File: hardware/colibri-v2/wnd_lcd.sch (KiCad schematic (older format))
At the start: 41 parts, among them CN6 Wurth-68715014522-LCD, U12 TSC2046IPWR

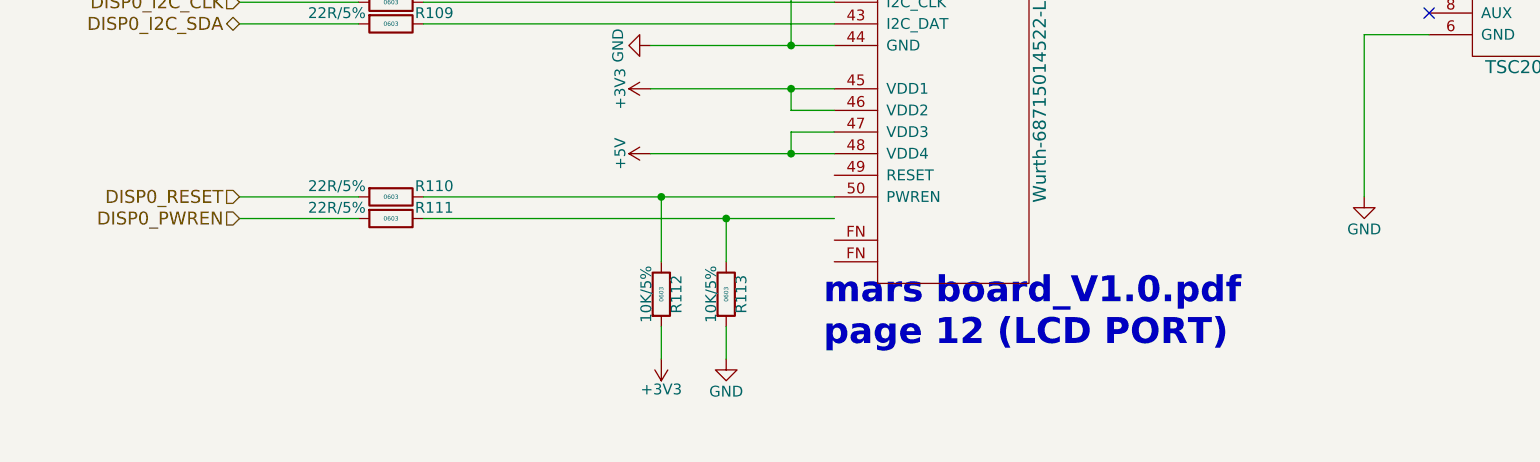
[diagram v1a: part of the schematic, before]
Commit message: Added footprints
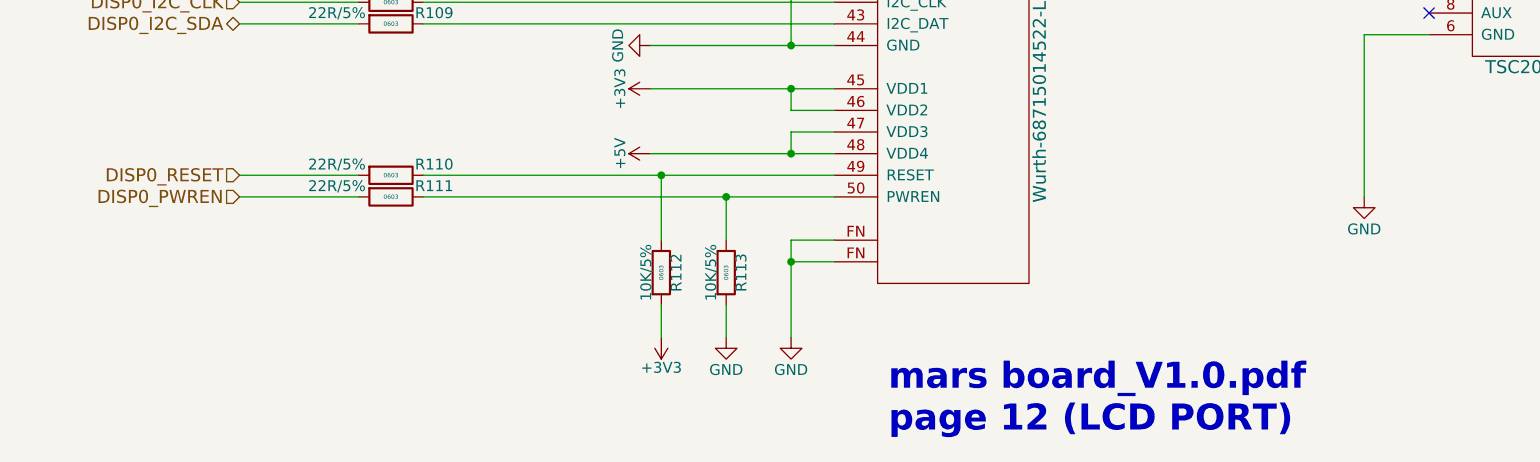
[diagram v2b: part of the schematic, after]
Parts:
- CN6: footprint (none) -> Sigmadrone:68715014522
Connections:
- net GND: now also CN6.FN
- net at CN6.49 (RESET): now also R110.1, R112.1
- net at R111.1, R113.1: now also CN6.50 (PWREN)
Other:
- moved on the sheet: R110, R111, R112, R113
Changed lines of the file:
@@
 F 0 "CN6" H 5300 6350 60  0000 C CNN
 F 1 "Wurth-68715014522-LCD" V 5500 1500 60  0000 C CNN
-F 2 "" H 5100 3900 60  0001 C CNN
+F 2 "Sigmadrone:68715014522" H 5100 3900 60  0001 C CNN
 F 3 "" H 5100 3900 60  0000 C CNN
 	1    5100 3550
@@
 $EndComp
 $Comp
-L GND #PWR0149
+L GND #PWR0150
 U 1 1 561E55DA
 P 7000 6100
-F 0 "#PWR0149" H 7000 5850 50  0001 C CNN
+F 0 "#PWR0150" H 7000 5850 50  0001 C CNN
 F 1 "GND" H 7000 5950 50  0000 C CNN
 F 2 "" H 7000 6100 60  0000 C CNN
@@
 $EndComp
 $Comp
-L +3V3 #PWR0150
+L +3V3 #PWR0151
 U 1 1 561E5805
 P 7000 4400
-F 0 "#PWR0150" H 7000 4250 50  0001 C CNN
+F 0 "#PWR0151" H 7000 4250 50  0001 C CNN
 F 1 "+3V3" H 7000 4540 50  0000 C CNN
 F 2 "" H 7000 4400 60  0000 C CNN
@@
 TOUCH_Y2
 $Comp
-L GND #PWR0151
+L GND #PWR0152
 U 1 1 561E5D84
 P 9300 6100
-F 0 "#PWR0151" H 9300 5850 50  0001 C CNN
+F 0 "#PWR0152" H 9300 5850 50  0001 C CNN
 F 1 "GND" H 9300 5950 50  0000 C CNN
 F 2 "" H 9300 6100 60  0000 C CNN
@@
 $EndComp
 $Comp
-L GND #PWR0152
+L GND #PWR0153
 U 1 1 561E5DA7
 P 9800 6100
-F 0 "#PWR0152" H 9800 5850 50  0001 C CNN
+F 0 "#PWR0153" H 9800 5850 50  0001 C CNN
 F 1 "GND" H 9800 5950 50  0000 C CNN
 F 2 "" H 9800 6100 60  0000 C CNN
@@
 $EndComp
 $Comp
-L +3V3 #PWR0153
+L +3V3 #PWR0154
 U 1 1 561E5EE9
 P 9800 3650
-F 0 "#PWR0153" H 9800 3500 50  0001 C CNN
+F 0 "#PWR0154" H 9800 3500 50  0001 C CNN
 F 1 "+3V3" H 9800 3790 50  0000 C CNN
 F 2 "" H 9800 3650 60  0000 C CNN
@@
 TOUCH_Y2
 $Comp
-L +3V3 #PWR0154
+L +3V3 #PWR0155
 U 1 1 561F4483
 P 3700 5600
-F 0 "#PWR0154" H 3700 5450 50  0001 C CNN
+F 0 "#PWR0155" H 3700 5450 50  0001 C CNN
 F 1 "+3V3" H 3700 5740 50  0000 C CNN
 F 2 "" H 3700 5600 60  0000 C CNN
@@
 $EndComp
 $Comp
-L +5V #PWR0155
+L +5V #PWR0156
 U 1 1 561F451C
 P 3700 5900
-F 0 "#PWR0155" H 3700 5750 50  0001 C CNN
+F 0 "#PWR0156" H 3700 5750 50  0001 C CNN
 F 1 "+5V" H 3700 6040 50  0000 C CNN
 F 2 "" H 3700 5900 60  0000 C CNN
@@
 $EndComp
 $Comp
-L +3V3 #PWR0156
+L +3V3 #PWR0157
 U 1 1 561F49E1
-P 3750 6850
-F 0 "#PWR0156" H 3750 6700 50  0001 C CNN
-F 1 "+3V3" H 3750 6990 50  0000 C CNN
-F 2 "" H 3750 6850 60  0000 C CNN
-F 3 "" H 3750 6850 60  0000 C CNN
-	1    3750 6850
+P 3750 6750
+F 0 "#PWR0157" H 3750 6600 50  0001 C CNN
+F 1 "+3V3" H 3750 6890 50  0000 C CNN
+F 2 "" H 3750 6750 60  0000 C CNN
+F 3 "" H 3750 6750 60  0000 C CNN
+	1    3750 6750
 	-1   0    0    1
 $EndComp
 $Comp
-L GND #PWR0157
+L GND #PWR0158
 U 1 1 561F4D74
-P 4050 6850
-F 0 "#PWR0157" H 4050 6600 50  0001 C CNN
-F 1 "GND" H 4050 6700 50  0000 C CNN
-F 2 "" H 4050 6850 60  0000 C CNN
-F 3 "" H 4050 6850 60  0000 C CNN
-	1    4050 6850
-	1    0    0    -1
-$EndComp
-Text HLabel 1800 6200 0    60   Input ~ 0
+P 4050 6750
+F 0 "#PWR0158" H 4050 6500 50  0001 C CNN
+F 1 "GND" H 4050 6600 50  0000 C CNN
+F 2 "" H 4050 6750 60  0000 C CNN
+F 3 "" H 4050 6750 60  0000 C CNN
+	1    4050 6750
+	1    0    0    -1
+$EndComp
+Text HLabel 1800 6100 0    60   Input ~ 0
 DISP0_PWREN
 Text HLabel 1800 4800 0    60   Input ~ 0
@@
 DISP0_I2C_SDA
 $Comp
-L GND #PWR0158
+L GND #PWR0159
 U 1 1 561F5E25
 P 3700 5400
-F 0 "#PWR0158" H 3700 5150 50  0001 C CNN
+F 0 "#PWR0159" H 3700 5150 50  0001 C CNN
 F 1 "GND" H 3700 5250 50  0000 C CNN
 F 2 "" H 3700 5400 60  0000 C CNN
@@
 	0    1    1    0
 $EndComp
-Text HLabel 1800 6100 0    60   Input ~ 0
+Text HLabel 1800 6000 0    60   Input ~ 0
 DISP0_RESET
 $Comp
-L +3V3 #PWR0159
+L +3V3 #PWR0160
 U 1 1 561F7FD1
 P 6400 800
-F 0 "#PWR0159" H 6400 650 50  0001 C CNN
+F 0 "#PWR0160" H 6400 650 50  0001 C CNN
 F 1 "+3V3" H 6400 940 50  0000 C CNN
 F 2 "" H 6400 800 60  0000 C CNN
@@
 $EndComp
 $Comp
-L GND #PWR0160
+L GND #PWR0161
 U 1 1 561F807C
 P 6400 1850
-F 0 "#PWR0160" H 6400 1600 50  0001 C CNN
+F 0 "#PWR0161" H 6400 1600 50  0001 C CNN
 F 1 "GND" H 6400 1700 50  0000 C CNN
 F 2 "" H 6400 1850 60  0000 C CNN
@@
 $EndComp
 $Comp
-L GND #PWR0161
+L GND #PWR0162
 U 1 1 561F88DD
 P 6400 3400
-F 0 "#PWR0161" H 6400 3150 50  0001 C CNN
+F 0 "#PWR0162" H 6400 3150 50  0001 C CNN
 F 1 "GND" H 6400 3250 50  0000 C CNN
 F 2 "" H 6400 3400 60  0000 C CNN
@@
 $EndComp
 $Comp
-L +5V #PWR0162
+L +5V #PWR0163
 U 1 1 561F8ABA
 P 6400 2350
-F 0 "#PWR0162" H 6400 2200 50  0001 C CNN
+F 0 "#PWR0163" H 6400 2200 50  0001 C CNN
 F 1 "+5V" H 6400 2490 50  0000 C CNN
 F 2 "" H 6400 2350 60  0000 C CNN
@@
 $EndComp
 $Comp
-L +3V3 #PWR0163
+L +3V3 #PWR0164
 U 1 1 561F8EEE
 P 9250 800
-F 0 "#PWR0163" H 9250 650 50  0001 C CNN
+F 0 "#PWR0164" H 9250 650 50  0001 C CNN
 F 1 "+3V3" H 9250 940 50  0000 C CNN
 F 2 "" H 9250 800 60  0000 C CNN
@@
 $EndComp
 $Comp
-L GND #PWR0164
+L GND #PWR0165
 U 1 1 561F8EF4
 P 9250 1850
-F 0 "#PWR0164" H 9250 1600 50  0001 C CNN
+F 0 "#PWR0165" H 9250 1600 50  0001 C CNN
 F 1 "GND" H 9250 1700 50  0000 C CNN
 F 2 "" H 9250 1850 60  0000 C CNN
@@
 	1    0    0    -1
 $EndComp
-Text Notes 4500 6800 0    120  ~ 24
+Text Notes 4800 7200 0    120  ~ 24
 mars board_V1.0.pdf\npage 12 (LCD PORT)
 Text HLabel 1800 3500 0    60   Input ~ 0
@@
 Research for \ncapacitive controller???
 $Comp
-L GND #PWR0165
+L GND #PWR0166
 U 1 1 5624CCFB
 P 1800 3300
-F 0 "#PWR0165" H 1800 3050 50  0001 C CNN
+F 0 "#PWR0166" H 1800 3050 50  0001 C CNN
 F 1 "GND" H 1800 3150 50  0000 C CNN
 F 2 "" H 1800 3300 60  0000 C CNN
@@
 Connection ~ 4350 5900
 Wire Wire Line
-	4050 6700 4050 6850
+	4050 6600 4050 6750
 Wire Wire Line
 	1800 4800 2350 4800
@@
 Connection ~ 4350 2600
 Wire Wire Line
-	3750 6700 3750 6850
+	3750 6600 3750 6750
+Wire Wire Line
+	2650 6000 4550 6000
 Wire Wire Line
 	2650 6100 4550 6100
 Wire Wire Line
-	2650 6200 4550 6200
+	1800 6000 2350 6000
 Wire Wire Line
 	1800 6100 2350 6100
 Wire Wire Line
-	1800 6200 2350 6200
-Wire Wire Line
-	4050 6400 4050 6200
-Connection ~ 4050 6200
-Wire Wire Line
-	3750 6400 3750 6100
-Connection ~ 3750 6100
+	4050 6300 4050 6100
+Connection ~ 4050 6100
+Wire Wire Line
+	3750 6300 3750 6000
+Connection ~ 3750 6000
 Wire Wire Line
 	7600 950  7600 1200
@@
 L R_SMT R111
 U 1 1 56341610
-P 2500 6200
-F 0 "R111" V 2450 6400 50  0000 C CNN
-F 1 "22R/5%" V 2450 5950 50  0000 C CNN
-F 2 "Resistors_SMD:R_0603" V 2650 6200 30  0001 C CNN
-F 3 "" V 2580 6200 30  0000 C CNN
-F 4 "0603" V 2500 6200 20  0000 C CNN "SMT"
-F 5 "9331891" V 2700 6200 30  0001 C CNN "Part"
-F 6 "Farnell" V 2750 6200 30  0001 C CNN "Provider"
-	1    2500 6200
-	0    1    1    0
-$EndComp
-$Comp
-L R_SMT R110
-U 1 1 56341B0D
 P 2500 6100
-F 0 "R110" V 2450 6300 50  0000 C CNN
+F 0 "R111" V 2450 6300 50  0000 C CNN
 F 1 "22R/5%" V 2450 5850 50  0000 C CNN
 F 2 "Resistors_SMD:R_0603" V 2650 6100 30  0001 C CNN
@@
 F 6 "Farnell" V 2750 6100 30  0001 C CNN "Provider"
 	1    2500 6100
+	0    1    1    0
+$EndComp
+$Comp
+L R_SMT R110
+U 1 1 56341B0D
+P 2500 6000
+F 0 "R110" V 2450 6200 50  0000 C CNN
+F 1 "22R/5%" V 2450 5750 50  0000 C CNN
+F 2 "Resistors_SMD:R_0603" V 2650 6000 30  0001 C CNN
+F 3 "" V 2580 6000 30  0000 C CNN
+F 4 "0603" V 2500 6000 20  0000 C CNN "SMT"
+F 5 "9331891" V 2700 6000 30  0001 C CNN "Part"
+F 6 "Farnell" V 2750 6000 30  0001 C CNN "Provider"
+	1    2500 6000
 	0    1    1    0
 $EndComp
@@
 L R_SMT R112
 U 1 1 56344727
-P 3750 6550
-F 0 "R112" V 3820 6550 50  0000 C CNN
-F 1 "10K/5%" V 3680 6550 50  0000 C CNN
-F 2 "Resistors_SMD:R_0603" V 3900 6550 30  0001 C CNN
-F 3 "" V 3830 6550 30  0000 C CNN
-F 4 "0603" V 3750 6550 20  0000 C CNN "SMT"
-F 5 "9331700" V 3950 6550 30  0001 C CNN "Part"
-F 6 "Farnell" V 4000 6550 30  0001 C CNN "Provider"
-	1    3750 6550
+P 3750 6450
+F 0 "R112" V 3820 6450 50  0000 C CNN
+F 1 "10K/5%" V 3680 6450 50  0000 C CNN
+F 2 "Resistors_SMD:R_0603" V 3900 6450 30  0001 C CNN
+F 3 "" V 3830 6450 30  0000 C CNN
+F 4 "0603" V 3750 6450 20  0000 C CNN "SMT"
+F 5 "9331700" V 3950 6450 30  0001 C CNN "Part"
+F 6 "Farnell" V 4000 6450 30  0001 C CNN "Provider"
+	1    3750 6450
 	1    0    0    -1
 $EndComp
@@
 L R_SMT R113
 U 1 1 56344972
-P 4050 6550
-F 0 "R113" V 4120 6550 50  0000 C CNN
-F 1 "10K/5%" V 3980 6550 50  0000 C CNN
-F 2 "Resistors_SMD:R_0603" V 4200 6550 30  0001 C CNN
-F 3 "" V 4130 6550 30  0000 C CNN
-F 4 "0603" V 4050 6550 20  0000 C CNN "SMT"
-F 5 "9331700" V 4250 6550 30  0001 C CNN "Part"
-F 6 "Farnell" V 4300 6550 30  0001 C CNN "Provider"
-	1    4050 6550
+P 4050 6450
+F 0 "R113" V 4120 6450 50  0000 C CNN
+F 1 "10K/5%" V 3980 6450 50  0000 C CNN
+F 2 "Resistors_SMD:R_0603" V 4200 6450 30  0001 C CNN
+F 3 "" V 4130 6450 30  0000 C CNN
+F 4 "0603" V 4050 6450 20  0000 C CNN "SMT"
+F 5 "9331700" V 4250 6450 30  0001 C CNN "Part"
+F 6 "Farnell" V 4300 6450 30  0001 C CNN "Provider"
+	1    4050 6450
 	1    0    0    -1
 $EndComp
@@
 TP_BUSY
 Connection ~ 9600 5050
+$Comp
+L GND #PWR0167
+U 1 1 56D2CBD4
+P 4350 6750
+F 0 "#PWR0167" H 4350 6500 50  0001 C CNN
+F 1 "GND" H 4350 6600 50  0000 C CNN
+F 2 "" H 4350 6750 60  0000 C CNN
+F 3 "" H 4350 6750 60  0000 C CNN
+	1    4350 6750
+	1    0    0    -1
+$EndComp
+Wire Wire Line
+	4550 6300 4350 6300
+Wire Wire Line
+	4350 6300 4350 6750
+Wire Wire Line
+	4550 6400 4350 6400
+Connection ~ 4350 6400
 $EndSCHEMATC

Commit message: Added footprints
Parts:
- U12: footprint (none) -> Housings_SSOP:TSSOP-16_4.4x5mm_Pitch0.65mm
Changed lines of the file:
@@
 F 0 "U12" H 8100 5500 60  0000 C CNN
 F 1 "TSC2046IPWR" H 7850 4500 60  0000 C CNN
-F 2 "" H 7850 4350 60  0001 C CNN
+F 2 "Housings_SSOP:TSSOP-16_4.4x5mm_Pitch0.65mm" H 7850 4350 60  0001 C CNN
 F 3 "" H 7850 4350 60  0000 C CNN
 	1    7850 5000
